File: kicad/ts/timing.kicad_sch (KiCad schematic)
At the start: 22 parts

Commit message: update footprints
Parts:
- F0, F2, G0, G1, G10, G4, G7, G8, G9, TS1: footprint (none) -> Package_DIP:DIP-14_W7.62mm
- N0: footprint (none) -> Package_DIP:DIP-16_W7.62mm
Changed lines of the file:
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@@
 			)
 		)
-		(property "Footprint" ""
+		(property "Footprint" "Package_DIP:DIP-14_W7.62mm"
 			(at 156.21 144.78 0)
 			(effects
@@
 			)
 		)
-		(property "Footprint" ""
+		(property "Footprint" "Package_DIP:DIP-14_W7.62mm"
 			(at 100.965 199.39 0)
 			(effects
@@
 			)
 		)
-		(property "Footprint" ""
+		(property "Footprint" "Package_DIP:DIP-14_W7.62mm"
 			(at 159.385 65.405 0)
 			(effects
@@
 			)
 		)
-		(property "Footprint" ""
+		(property "Footprint" "Package_DIP:DIP-14_W7.62mm"
 			(at 50.165 60.325 0)
 			(effects
@@
 			)
 		)
-		(property "Footprint" ""
+		(property "Footprint" "Package_DIP:DIP-14_W7.62mm"
 			(at 78.105 113.03 0)
 			(effects
@@
 			)
 		)
-		(property "Footprint" ""
+		(property "Footprint" "Package_DIP:DIP-14_W7.62mm"
 			(at 72.39 101.6 0)
 			(effects
@@
 			)
 		)
-		(property "Footprint" ""
+		(property "Footprint" "Package_DIP:DIP-14_W7.62mm"
 			(at 66.675 60.325 0)
 			(effects
@@
 			)
 		)
-		(property "Footprint" ""
+		(property "Footprint" "Package_DIP:DIP-14_W7.62mm"
 			(at 142.875 50.165 0)
 			(effects
@@
 			)
 		)
-		(property "Footprint" ""
+		(property "Footprint" "Package_DIP:DIP-14_W7.62mm"
 			(at 139.065 110.49 0)
 			(effects
@@
 			)
 		)
-		(property "Footprint" ""
+		(property "Footprint" "Package_DIP:DIP-14_W7.62mm"
 			(at 64.77 140.335 0)
 			(effects
@@
 			)
 		)
-		(property "Footprint" ""
+		(property "Footprint" "Package_DIP:DIP-14_W7.62mm"
 			(at 39.37 120.65 0)
 			(effects
@@
 			)
 		)
-		(property "Footprint" ""
+		(property "Footprint" "Package_DIP:DIP-14_W7.62mm"
 			(at 74.93 236.22 0)
 			(effects
@@
 			)
 		)
-		(property "Footprint" ""
+		(property "Footprint" "Package_DIP:DIP-14_W7.62mm"
 			(at 106.045 156.845 0)
 			(effects
@@
 			)
 		)
-		(property "Footprint" ""
+		(property "Footprint" "Package_DIP:DIP-14_W7.62mm"
 			(at 139.065 101.6 0)
 			(effects
@@
 			)
 		)
-		(property "Footprint" ""
+		(property "Footprint" "Package_DIP:DIP-14_W7.62mm"
 			(at 142.875 124.46 0)
 			(effects
@@
 			)
 		)
-		(property "Footprint" ""
+		(property "Footprint" "Package_DIP:DIP-14_W7.62mm"
 			(at 129.54 33.02 0)
 			(effects
@@
 			)
 		)
-		(property "Footprint" ""
+		(property "Footprint" "Package_DIP:DIP-14_W7.62mm"
 			(at 97.155 104.14 0)
 			(effects
@@
 			)
 		)
-		(property "Footprint" ""
+		(property "Footprint" "Package_DIP:DIP-14_W7.62mm"
 			(at 135.89 205.74 0)
 			(effects
@@
 			)
 		)
-		(property "Footprint" ""
+		(property "Footprint" "Package_DIP:DIP-14_W7.62mm"
 			(at 42.545 137.795 0)
 			(effects
@@
 			)
 		)
-		(property "Footprint" ""
+		(property "Footprint" "Package_DIP:DIP-14_W7.62mm"
 			(at 145.415 160.02 0)
 			(effects
@@
 			)
 		)
-		(property "Footprint" ""
+		(property "Footprint" "Package_DIP:DIP-16_W7.62mm"
 			(at 93.98 52.705 0)
 			(effects
@@
 			)
 		)
-		(property "Footprint" ""
+		(property "Footprint" "Package_DIP:DIP-14_W7.62mm"
 			(at 41.275 110.49 0)
 			(effects
@@
 			)
 		)
-		(property "Footprint" ""
+		(property "Footprint" "Package_DIP:DIP-14_W7.62mm"
 			(at 120.65 121.92 0)
 			(effects
@@
 			)
 		)
-		(property "Footprint" ""
+		(property "Footprint" "Package_DIP:DIP-14_W7.62mm"
 			(at 33.655 60.325 0)
 			(effects
@@
 			)
 		)
-		(property "Footprint" ""
+		(property "Footprint" "Package_DIP:DIP-14_W7.62mm"
 			(at 41.275 99.06 0)
 			(effects
@@
 			)
 		)
-		(property "Footprint" ""
+		(property "Footprint" "Package_DIP:DIP-14_W7.62mm"
 			(at 58.42 123.19 0)
 			(effects
@@
 			)
 		)
-		(property "Footprint" ""
+		(property "Footprint" "Package_DIP:DIP-14_W7.62mm"
 			(at 118.11 101.6 0)
 			(effects
@@
 			)
 		)
-		(property "Footprint" ""
+		(property "Footprint" "Package_DIP:DIP-14_W7.62mm"
 			(at 98.425 216.535 0)
 			(effects
@@
 			)
 		)
-		(property "Footprint" ""
+		(property "Footprint" "Package_DIP:DIP-14_W7.62mm"
 			(at 74.295 225.425 0)
 			(effects
@@
 			)
 		)
-		(property "Footprint" ""
+		(property "Footprint" "Package_DIP:DIP-14_W7.62mm"
 			(at 74.295 213.995 0)
 			(effects

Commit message: Schemativ corrections, work started on pcb
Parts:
- G5: footprint (none) -> Package_DIP:DIP-14_W7.62mm
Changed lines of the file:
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@@
 			)
 		)
-		(property "Footprint" ""
+		(property "Footprint" "Package_DIP:DIP-14_W7.62mm"
 			(at 167.005 45.085 0)
 			(effects

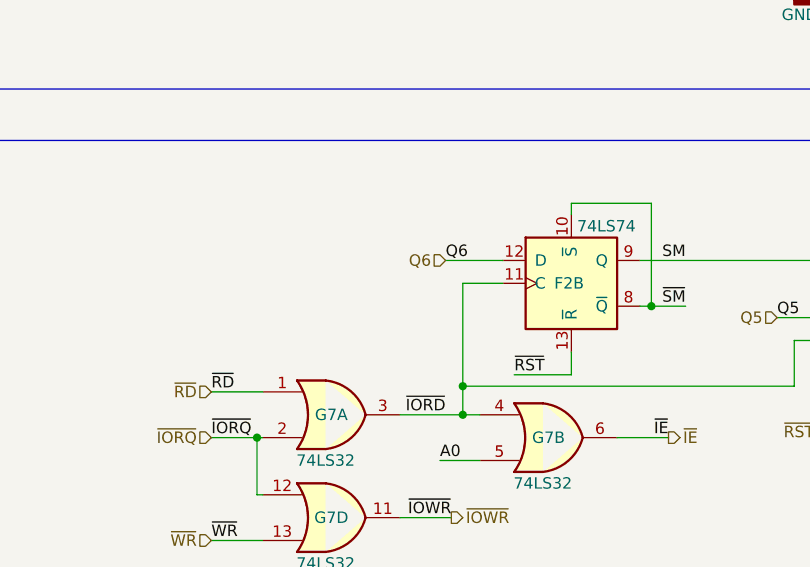
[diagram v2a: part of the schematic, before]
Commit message: Schematic corrections, more traces to pcb, update to DIN 3x32 connector footprint
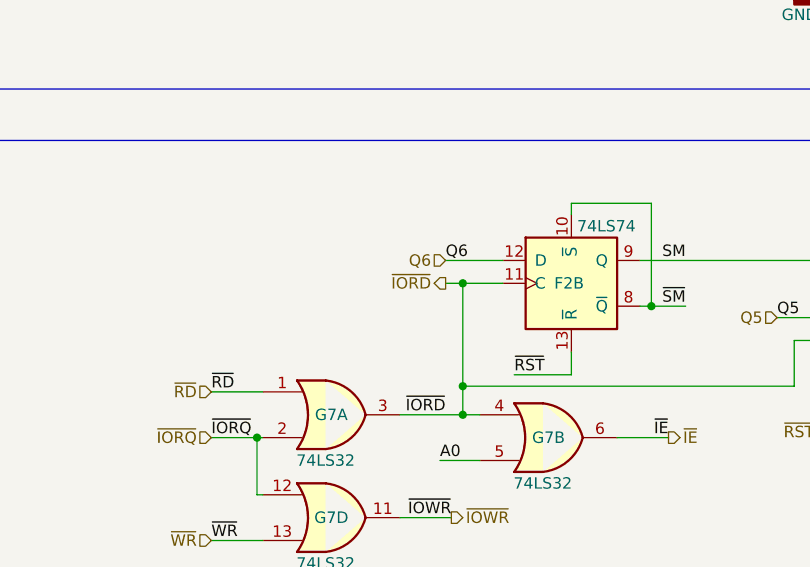
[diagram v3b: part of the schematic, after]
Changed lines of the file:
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@@
+	)
+	(junction
+		(at 88.9 199.39)
+		(diameter 0)
+		(color 0 0 0 0)
 	)
 	(junction
@@
 	(wire
 		(pts
+			(xy 86.995 199.39) (xy 88.9 199.39)
+		)
+		(stroke
+			(width 0)
+			(type default)
+		)
+	)
+	(wire
+		(pts
 			(xy 46.99 120.65) (xy 50.8 120.65)
 		)
@@
 		)
 	)
+	(hierarchical_label "~{IORD}"
+		(shape output)
+		(at 86.995 199.39 180)
+		(fields_autoplaced yes)
+		(effects
+			(font
+				(size 1.27 1.27)
+			)
+			(justify right)
+		)
+	)

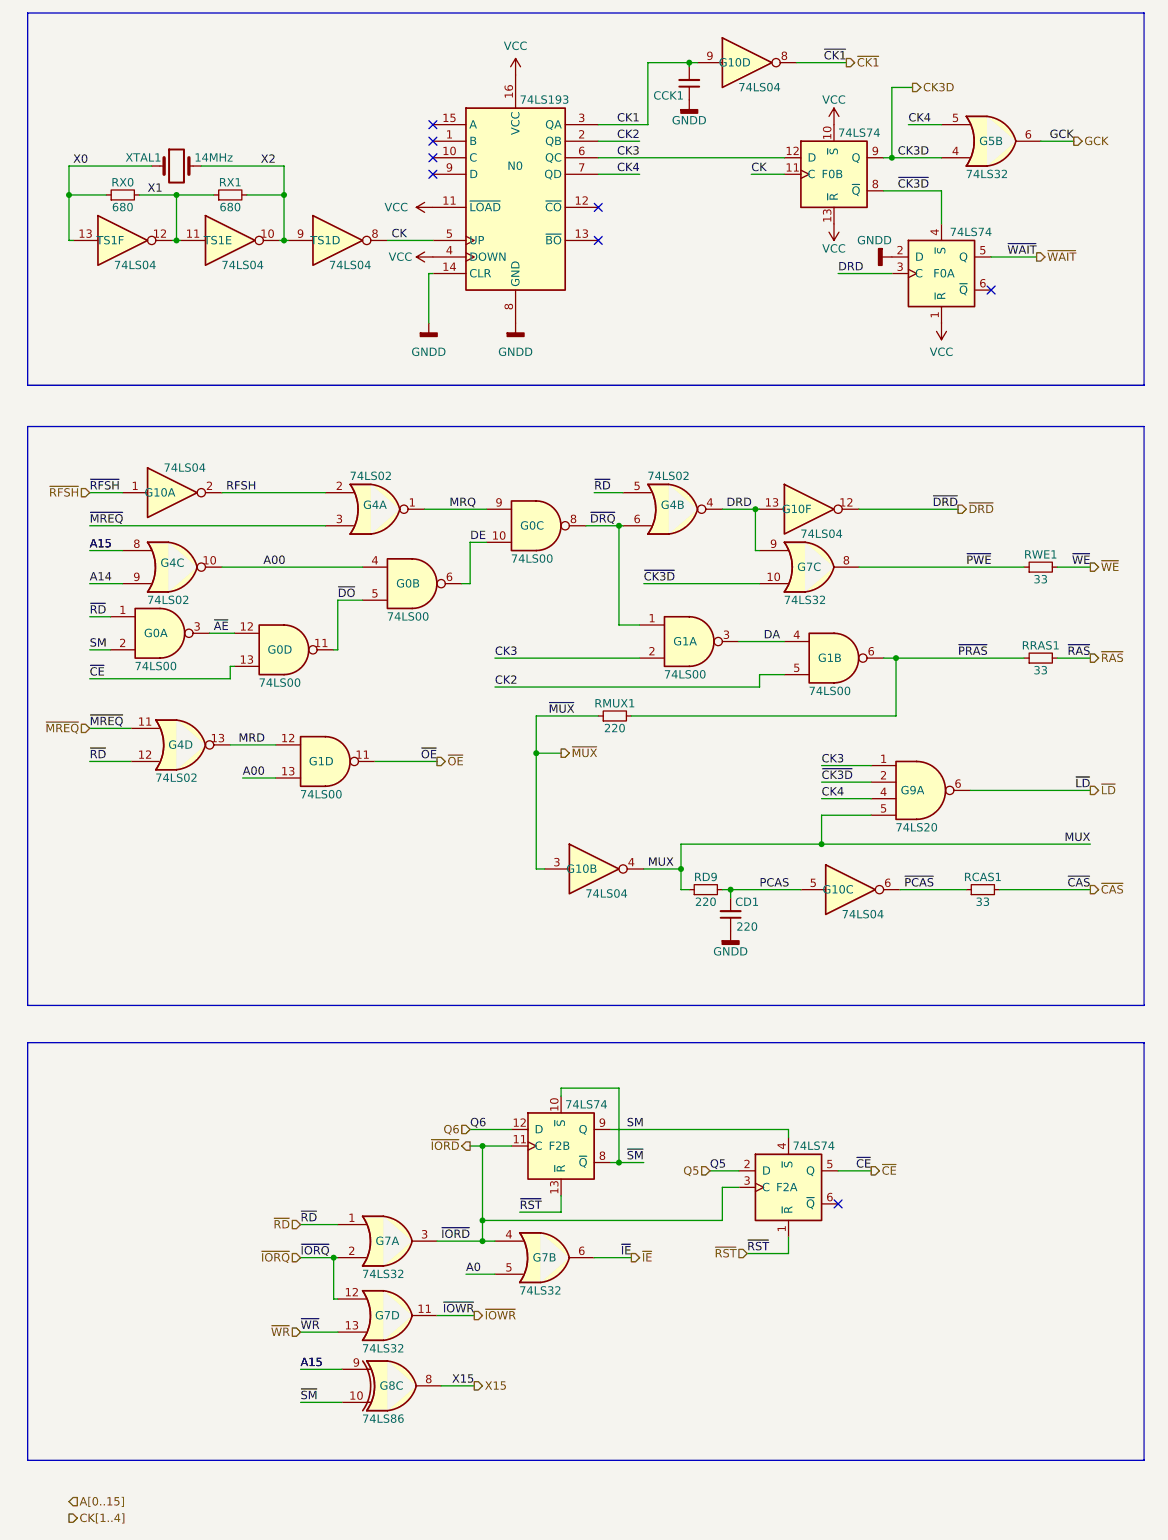
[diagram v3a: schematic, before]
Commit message: Schematic corrections, more traces to pcb
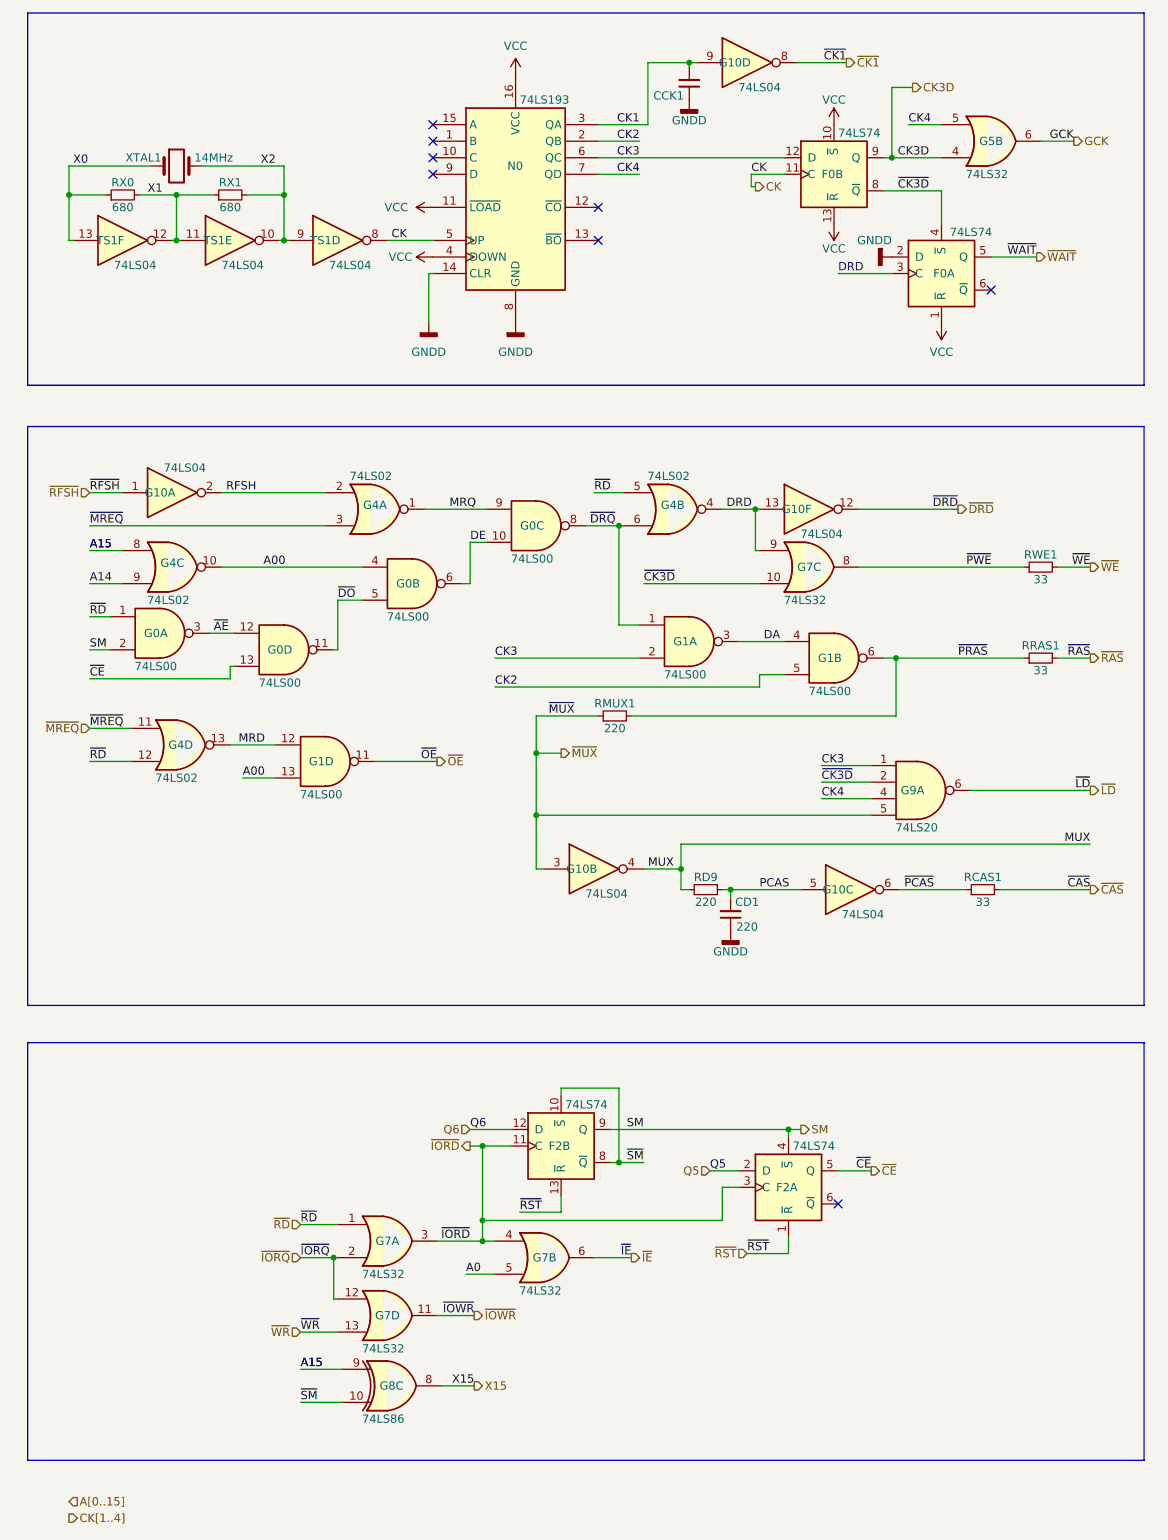
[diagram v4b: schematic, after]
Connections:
- net MUX: no longer G9.5
- net ~{MUX}: now also G9.5
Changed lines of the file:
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@@
+	)
+	(junction
+		(at 97.155 148.59)
+		(diameter 0)
+		(color 0 0 0 0)
 	)
 	(junction
@@
 	)
 	(junction
-		(at 140.97 153.035)
-		(diameter 0)
-		(color 0 0 0 0)
-	)
-	(junction
 		(at 109.855 104.14)
 		(diameter 0)
@@
 	)
 	(junction
+		(at 135.89 196.85)
+		(diameter 0)
+		(color 0 0 0 0)
+	)
+	(junction
 		(at 109.855 201.93)
 		(diameter 0)
@@
 	(wire
 		(pts
-			(xy 97.155 139.065) (xy 97.155 156.845)
+			(xy 97.155 139.065) (xy 97.155 148.59)
 		)
 		(stroke
@@
 	(wire
 		(pts
+			(xy 130.175 52.07) (xy 130.175 50.165)
+		)
+		(stroke
+			(width 0)
+			(type default)
+		)
+	)
+	(wire
+		(pts
 			(xy 25.4 48.895) (xy 38.1 48.895)
 		)
@@
 	(wire
 		(pts
+			(xy 135.89 196.85) (xy 137.795 196.85)
+		)
+		(stroke
+			(width 0)
+			(type default)
+		)
+	)
+	(wire
+		(pts
 			(xy 28.575 135.255) (xy 34.925 135.255)
 		)
@@
 	(wire
 		(pts
-			(xy 140.97 148.59) (xy 140.97 153.035)
-		)
-		(stroke
-			(width 0)
-			(type default)
-		)
-	)
-	(wire
-		(pts
 			(xy 25.4 60.325) (xy 26.035 60.325)
 		)
@@
 	(wire
 		(pts
+			(xy 130.81 52.07) (xy 130.175 52.07)
+		)
+		(stroke
+			(width 0)
+			(type default)
+		)
+	)
+	(wire
+		(pts
 			(xy 88.9 210.82) (xy 88.9 213.995)
 		)
@@
 	(wire
 		(pts
-			(xy 140.97 148.59) (xy 148.59 148.59)
-		)
-		(stroke
-			(width 0)
-			(type default)
-		)
-	)
-	(wire
-		(pts
 			(xy 48.895 99.06) (xy 64.77 99.06)
 		)
@@
 	(wire
 		(pts
+			(xy 97.155 148.59) (xy 97.155 156.845)
+		)
+		(stroke
+			(width 0)
+			(type default)
+		)
+	)
+	(wire
+		(pts
 			(xy 86.995 106.68) (xy 86.995 113.03)
 		)
@@
 	(wire
 		(pts
-			(xy 140.97 153.035) (xy 182.245 153.035)
-		)
-		(stroke
-			(width 0)
-			(type default)
-		)
-	)
-	(wire
-		(pts
 			(xy 123.825 203.2) (xy 128.27 203.2)
 		)
@@
 	(wire
 		(pts
+			(xy 97.155 148.59) (xy 148.59 148.59)
+		)
+		(stroke
+			(width 0)
+			(type default)
+		)
+	)
+	(wire
+		(pts
 			(xy 94.615 209.55) (xy 100.965 209.55)
 		)
@@
 	(wire
 		(pts
-			(xy 119.38 153.035) (xy 140.97 153.035)
+			(xy 119.38 153.035) (xy 182.245 153.035)
 		)
 		(stroke
@@
 		)
 	)
+	(hierarchical_label "SM"
+		(shape output)
+		(at 137.795 196.85 0)
+		(fields_autoplaced yes)
+		(effects
+			(font
+				(size 1.27 1.27)
+			)
+			(justify left)
+		)
+	)
 	(hierarchical_label "~{OE}"
 		(shape output)
@@
 		(fields_autoplaced yes)
 		(effects
+			(font
+				(size 1.27 1.27)
+			)
+			(justify left)
+		)
+	)
+	(hierarchical_label "CK"
+		(shape output)
+		(at 130.81 52.07 0)
+		(fields_autoplaced yes)
+		(effects

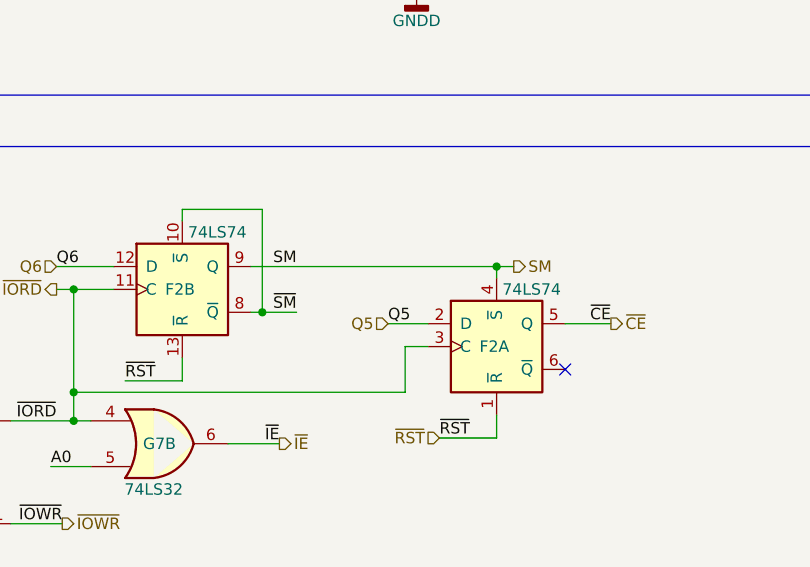
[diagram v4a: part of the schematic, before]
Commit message: Schematic corrections, all pcb traces placed, todo footprints check
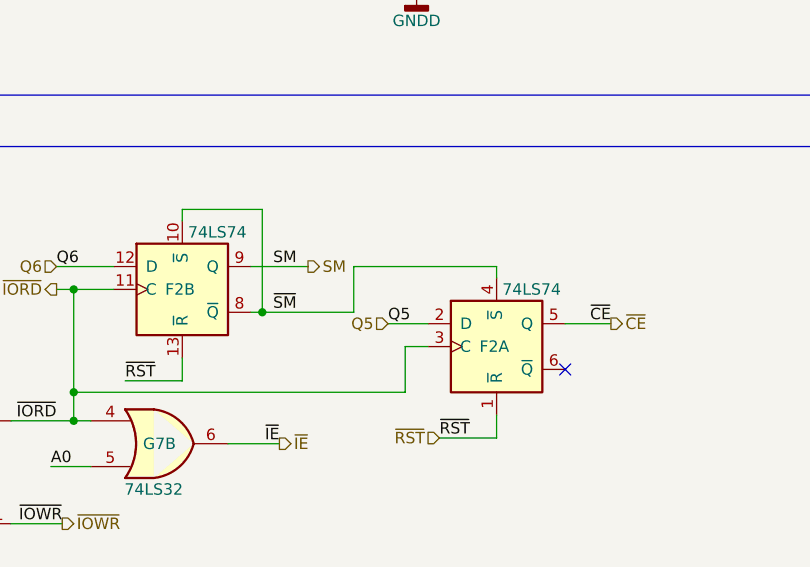
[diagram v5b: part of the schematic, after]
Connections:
- net SM: no longer F2.4 (~{S})
- net ~{SM}: now also F2.4 (~{S})
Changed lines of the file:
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@@
-	)
-	(junction
-		(at 135.89 196.85)
-		(diameter 0)
-		(color 0 0 0 0)
 	)
 	(junction
@@
 	(wire
 		(pts
-			(xy 108.585 196.85) (xy 135.89 196.85)
+			(xy 108.585 196.85) (xy 114.935 196.85)
 		)
 		(stroke
@@
 	(wire
 		(pts
-			(xy 135.89 196.85) (xy 137.795 196.85)
-		)
-		(stroke
-			(width 0)
-			(type default)
-		)
-	)
-	(wire
-		(pts
 			(xy 28.575 135.255) (xy 34.925 135.255)
 		)
@@
 	(wire
 		(pts
-			(xy 135.89 198.12) (xy 135.89 196.85)
+			(xy 120.015 196.85) (xy 135.89 196.85)
 		)
 		(stroke
@@
 	(wire
 		(pts
+			(xy 120.015 201.93) (xy 120.015 196.85)
+		)
+		(stroke
+			(width 0)
+			(type default)
+		)
+	)
+	(wire
+		(pts
 			(xy 28.575 118.11) (xy 31.75 118.11)
 		)
@@
 	(wire
 		(pts
-			(xy 109.855 201.93) (xy 113.665 201.93)
+			(xy 109.855 201.93) (xy 120.015 201.93)
 		)
 		(stroke
@@
 		(pts
 			(xy 97.155 148.59) (xy 148.59 148.59)
+		)
+		(stroke
+			(width 0)
+			(type default)
+		)
+	)
+	(wire
+		(pts
+			(xy 135.89 196.85) (xy 135.89 198.12)
 		)
 		(stroke
@@
 	(hierarchical_label "SM"
 		(shape output)
-		(at 137.795 196.85 0)
-		(fields_autoplaced yes)
-		(effects
+		(at 114.935 196.85 0)
+		(fields_autoplaced yes)
+		(effects
